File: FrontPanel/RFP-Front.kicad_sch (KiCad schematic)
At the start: 20 parts, among them J1 COMM, J2 SWD, J3 BUZZ / BTNLED, U1 STM32F103C8T6, U2 OLED_128x64

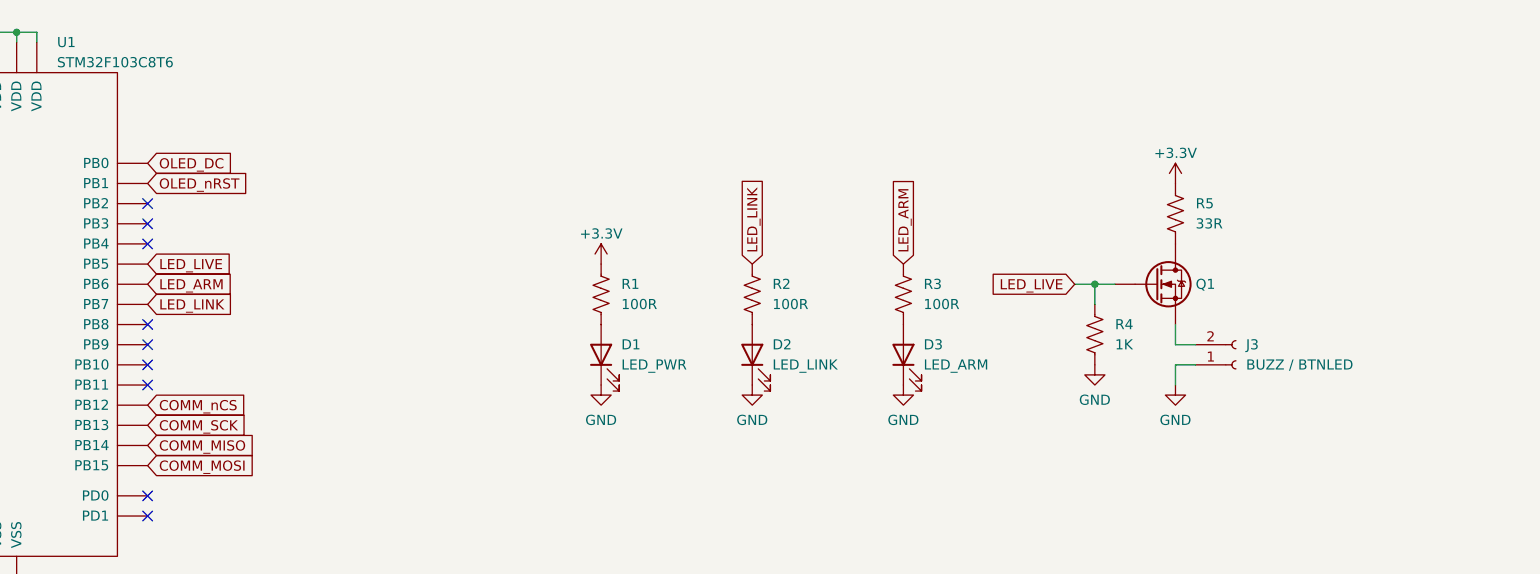
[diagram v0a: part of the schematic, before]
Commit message: Rearrange and dim LEDs
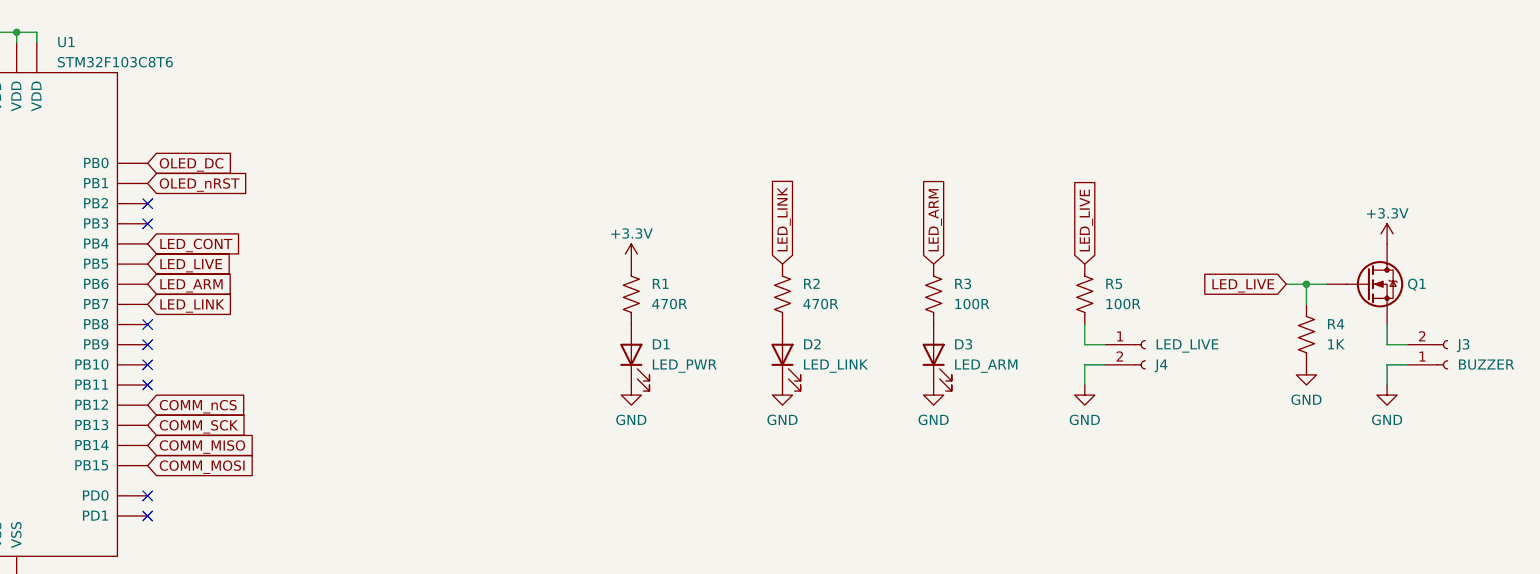
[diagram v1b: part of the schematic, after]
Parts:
- added J4: LED_LIVE, Resistor_SMD:R_2512_6332Metric, symbol Connector:Conn_01x02_Female
- J3: value BUZZ / BTNLED -> BUZZER
- R1, R2: value 100R -> 470R; Part# Generic 100R 0402 Resistor -> Generic 470R 0402 Resistor
- R5: value 33R -> 100R; Part# Generic 33R 0402 Resistor -> Generic 100R 0402 Resistor
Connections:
- net +3.3V: now also Q1.3 (D); no longer R5.1
- net GND: now also J4.2 (Pin_2)
- net LED_LIVE: now also R5.1
- net LED_CONT: now reaches U1.40 (PB4)
- net at R5.2: now also J4.1 (Pin_1); no longer Q1.3 (D)
- no-connect marks 21 -> 20
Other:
- moved on the sheet: D1, D2, D3, J3, Q1, R1, R2, R3, R4, R5
